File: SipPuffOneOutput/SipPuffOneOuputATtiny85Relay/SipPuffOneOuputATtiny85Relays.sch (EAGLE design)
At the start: 13 parts, among them U1 ATTINY85-20PU, U2 AQY212EH

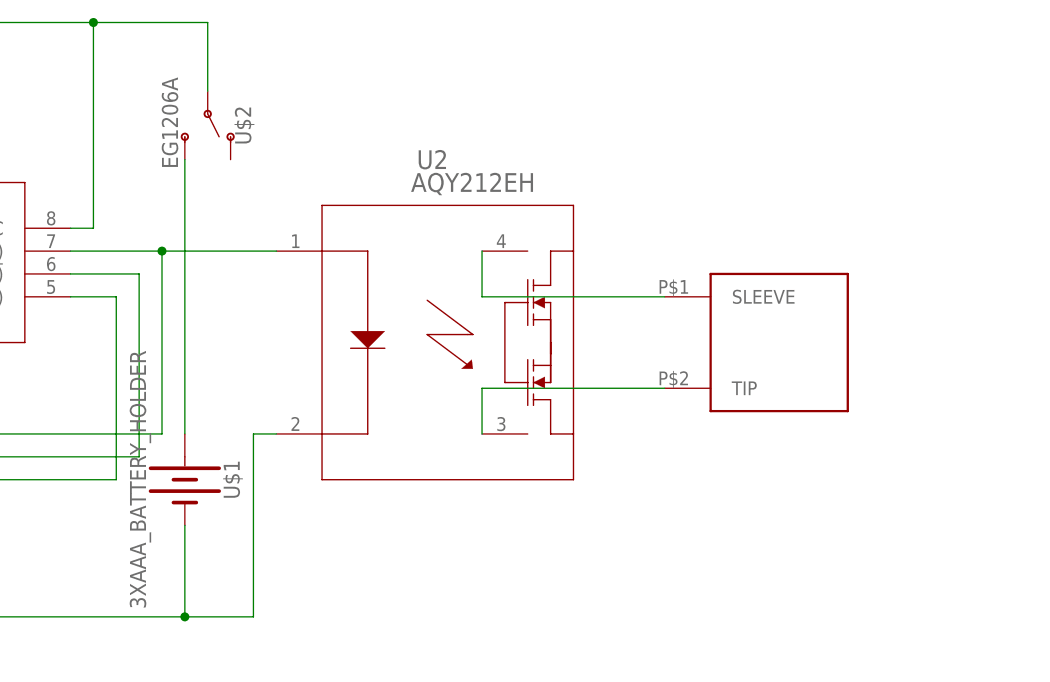
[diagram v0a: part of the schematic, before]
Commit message: Changed resistors size
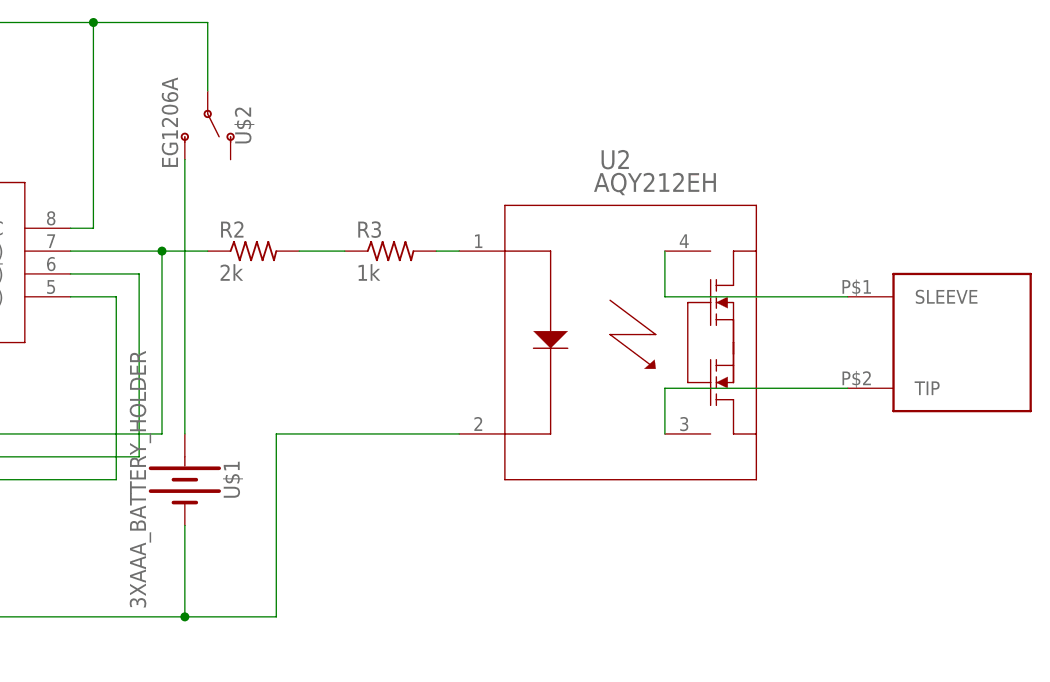
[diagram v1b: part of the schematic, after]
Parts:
- added R2: 2k, MMC Eagle:RESISTOR_R-US_
- added R3: 1k, MMC Eagle:RESISTOR_R-US_
- R1: device MMC Eagle:RESISTOR_R-US_0204/7 -> MMC Eagle:RESISTOR_R-US_
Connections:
- new net N$11: R2.2, R3.1
- new net N$14: R3.2, U2.1
- net N$6: now also R2.1; no longer U2.1
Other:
- moved on the sheet: U2
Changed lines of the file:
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@@
 <part name="C2" library="MMC Eagle" library_urn="urn:adsk.eagle:library:3491419" deviceset="0.1UF" device="-KIT-EZ-50V-20%" package3d_urn="urn:adsk.eagle:package:3493607/2" value="0.01uF"/>
 <part name="C3" library="MMC Eagle" library_urn="urn:adsk.eagle:library:3491419" deviceset="0.1UF" device="-KIT-EZ-50V-20%" package3d_urn="urn:adsk.eagle:package:3493607/2" value="1uF"/>
-<part name="R1" library="MMC Eagle" library_urn="urn:adsk.eagle:library:3491419" deviceset="RESISTOR_R-US_" device="0204/7" package3d_urn="urn:adsk.eagle:package:3491542/2"/>
+<part name="R1" library="MMC Eagle" library_urn="urn:adsk.eagle:library:3491419" deviceset="RESISTOR_R-US_" device="" package3d_urn="urn:adsk.eagle:package:5426338/2"/>
 <part name="D1" library="MMC Eagle" library_urn="urn:adsk.eagle:library:3491419" deviceset="LED" device="5MM" package3d_urn="urn:adsk.eagle:package:3634149/2"/>
 <part name="GND1" library="MMC Eagle" library_urn="urn:adsk.eagle:library:3491419" deviceset="GND" device=""/>
@@
 <part name="U$4" library="MMC Eagle" library_urn="urn:adsk.eagle:library:3491419" deviceset="HEADER_2X03" device="" package3d_urn="urn:adsk.eagle:package:4704386/2"/>
 <part name="U$5" library="MMC Eagle" library_urn="urn:adsk.eagle:library:3491419" deviceset="HEADER_1X02" device="" package3d_urn="urn:adsk.eagle:package:4737896/2"/>
+<part name="R2" library="MMC Eagle" library_urn="urn:adsk.eagle:library:3491419" deviceset="RESISTOR_R-US_" device="" package3d_urn="urn:adsk.eagle:package:5426338/2" value="2k"/>
+<part name="R3" library="MMC Eagle" library_urn="urn:adsk.eagle:library:3491419" deviceset="RESISTOR_R-US_" device="" package3d_urn="urn:adsk.eagle:package:5426338/2" value="1k"/>
 </parts>
 <sheets>
@@
 <instance part="U$1" gate="G$1" x="264.16" y="12.7" rot="R270"/>
 <instance part="U$2" gate="G$1" x="266.7" y="53.34" rot="R270"/>
-<instance part="U$3" gate="G$1" x="330.2" y="27.94"/>
-<instance part="U2" gate="A" x="271.78" y="38.1"/>
+<instance part="U$3" gate="G$1" x="350.52" y="27.94"/>
+<instance part="U2" gate="A" x="292.1" y="38.1"/>
 <instance part="U$4" gate="A" x="144.78" y="15.24"/>
 <instance part="U$5" gate="G$1" x="53.34" y="55.88" rot="R180"/>
+<instance part="R2" gate="G$1" x="271.78" y="38.1"/>
+<instance part="R3" gate="G$1" x="287.02" y="38.1"/>
 </instances>
 <busses>
@@
 <wire x1="264.16" y1="-2.54" x2="43.18" y2="-2.54" width="0.1524" layer="91"/>
 <junction x="43.18" y="-2.54"/>
-<pinref part="U2" gate="A" pin="2"/>
-<wire x1="274.32" y1="17.78" x2="271.78" y2="17.78" width="0.1524" layer="91"/>
-<wire x1="271.78" y1="17.78" x2="271.78" y2="-2.54" width="0.1524" layer="91"/>
-<wire x1="271.78" y1="-2.54" x2="264.16" y2="-2.54" width="0.1524" layer="91"/>
-<junction x="264.16" y="-2.54"/>
 <pinref part="U$4" gate="A" pin="3"/>
 <wire x1="137.16" y1="15.24" x2="43.18" y2="15.24" width="0.1524" layer="91"/>
 <junction x="43.18" y="15.24"/>
+<pinref part="U2" gate="A" pin="2"/>
+<wire x1="294.64" y1="17.78" x2="274.32" y2="17.78" width="0.1524" layer="91"/>
+<wire x1="274.32" y1="17.78" x2="274.32" y2="-2.54" width="0.1524" layer="91"/>
+<wire x1="274.32" y1="-2.54" x2="264.16" y2="-2.54" width="0.1524" layer="91"/>
+<junction x="264.16" y="-2.54"/>
 </segment>
 </net>
@@
 <segment>
 <pinref part="U1" gate="A" pin="PB2_(SCK/USCK/SCL/ADC1/T0/INT0/PCINT2)"/>
-<pinref part="U2" gate="A" pin="1"/>
 <wire x1="251.46" y1="38.1" x2="261.62" y2="38.1" width="0.1524" layer="91"/>
 <pinref part="U$4" gate="A" pin="2"/>
-<wire x1="261.62" y1="38.1" x2="274.32" y2="38.1" width="0.1524" layer="91"/>
 <wire x1="152.4" y1="17.78" x2="261.62" y2="17.78" width="0.1524" layer="91"/>
 <wire x1="261.62" y1="17.78" x2="261.62" y2="38.1" width="0.1524" layer="91"/>
+<pinref part="R2" gate="G$1" pin="1"/>
+<wire x1="266.7" y1="38.1" x2="261.62" y2="38.1" width="0.1524" layer="91"/>
 <junction x="261.62" y="38.1"/>
 </segment>
@@
 <pinref part="U2" gate="A" pin="4"/>
 <pinref part="U$3" gate="G$1" pin="SLEEVE"/>
-<wire x1="297.18" y1="38.1" x2="297.18" y2="33.02" width="0.1524" layer="91"/>
-<wire x1="297.18" y1="33.02" x2="317.5" y2="33.02" width="0.1524" layer="91"/>
+<wire x1="317.5" y1="38.1" x2="317.5" y2="33.02" width="0.1524" layer="91"/>
+<wire x1="317.5" y1="33.02" x2="337.82" y2="33.02" width="0.1524" layer="91"/>
 </segment>
 </net>
@@
 <pinref part="U2" gate="A" pin="3"/>
 <pinref part="U$3" gate="G$1" pin="TIP"/>
-<wire x1="297.18" y1="17.78" x2="297.18" y2="22.86" width="0.1524" layer="91"/>
-<wire x1="297.18" y1="22.86" x2="317.5" y2="22.86" width="0.1524" layer="91"/>
+<wire x1="317.5" y1="17.78" x2="317.5" y2="22.86" width="0.1524" layer="91"/>
+<wire x1="317.5" y1="22.86" x2="337.82" y2="22.86" width="0.1524" layer="91"/>
 </segment>
 </net>
@@
 </segment>
 </net>
+<net name="N$11" class="0">
+<segment>
+<pinref part="R2" gate="G$1" pin="2"/>
+<pinref part="R3" gate="G$1" pin="1"/>
+<wire x1="276.86" y1="38.1" x2="281.94" y2="38.1" width="0.1524" layer="91"/>
+</segment>
+</net>
+<net name="N$14" class="0">
+<segment>
+<pinref part="R3" gate="G$1" pin="2"/>
+<pinref part="U2" gate="A" pin="1"/>
+<wire x1="292.1" y1="38.1" x2="294.64" y2="38.1" width="0.1524" layer="91"/>
+</segment>
+</net>
